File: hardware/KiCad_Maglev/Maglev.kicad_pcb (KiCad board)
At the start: 2 copper layers, 120 x 120 mm, 69 parts, among them IC1 TLV1117LV33DCYR, J1 USB_C_Receptacle, J2 62100421921, J3 61300311121, J4 694106301002, J5 621008245821, J6 621006245821, U1 ESP32-C3, U2 TMAG5173A2QDBVRQ1, Y2 IQXC-42_830108213209

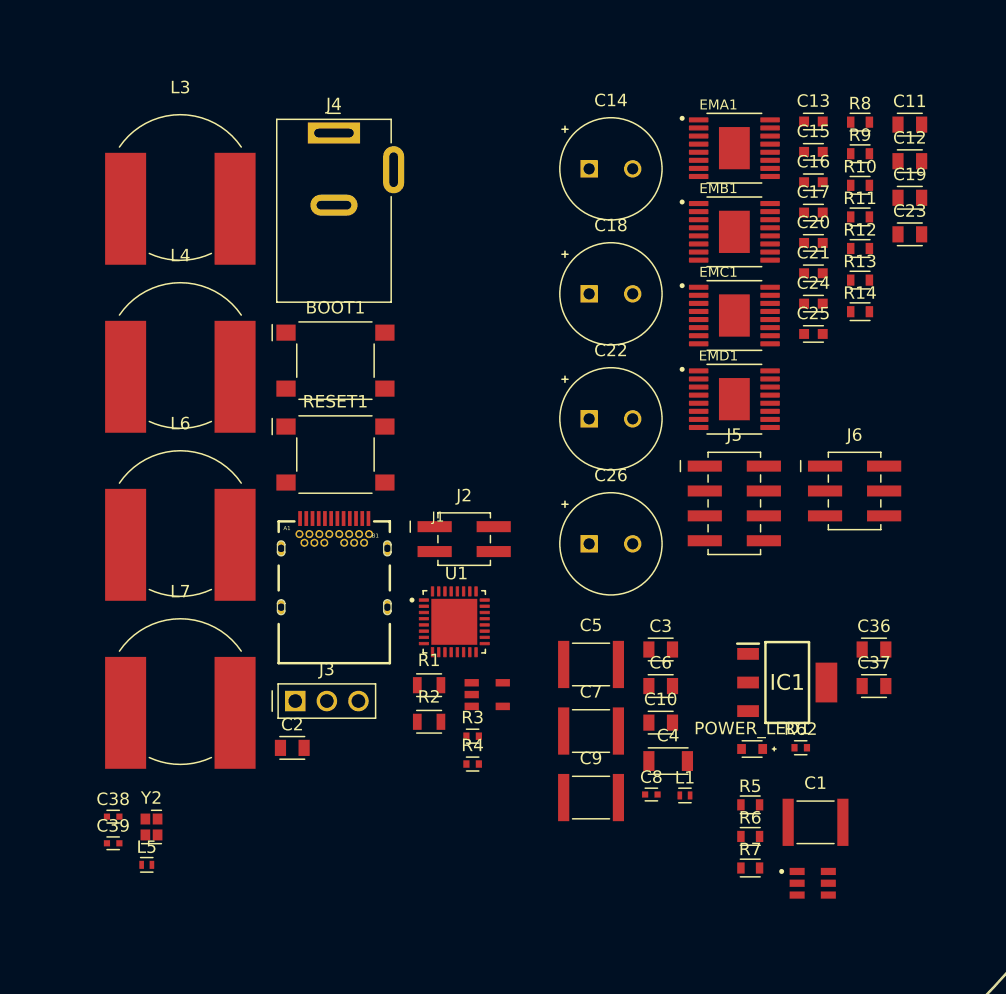
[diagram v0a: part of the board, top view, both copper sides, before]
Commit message: some changes to pcb schmatic, added datasheets for used components and linked wurth repo
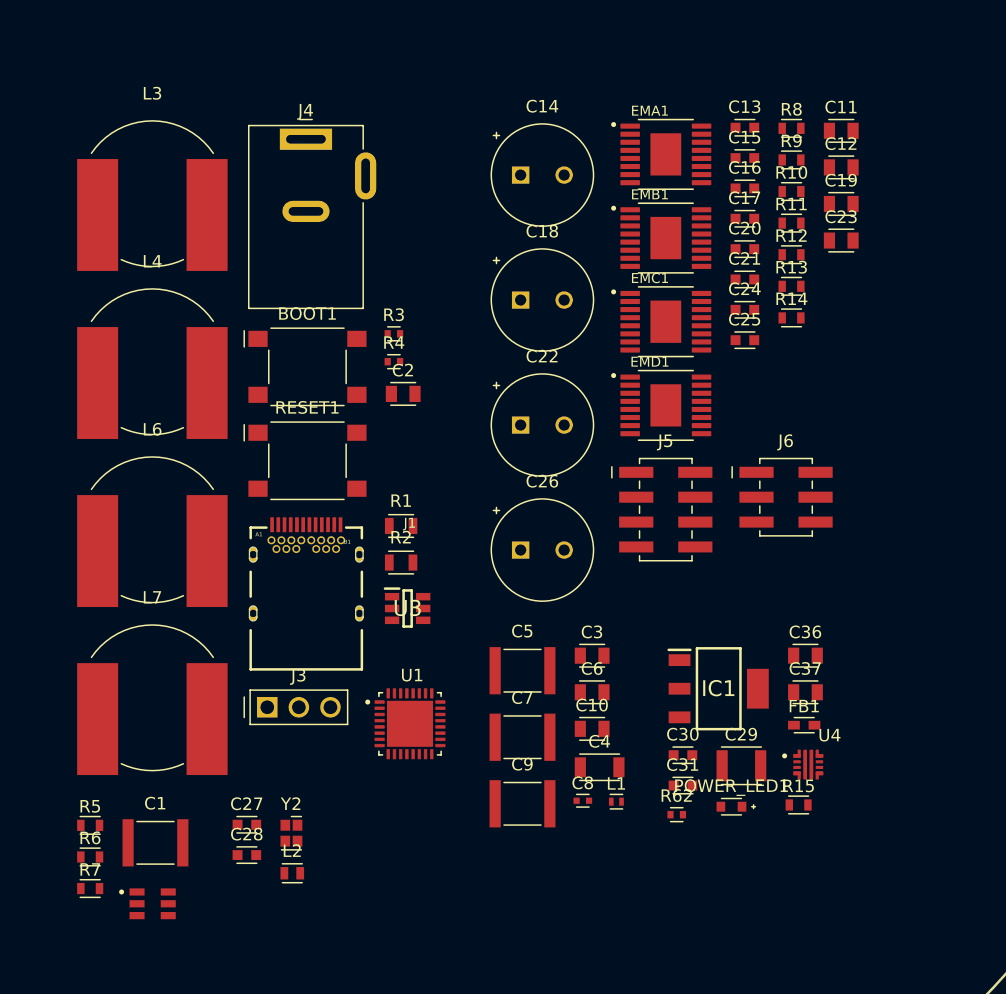
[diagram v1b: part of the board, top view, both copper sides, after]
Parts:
- removed C38, C39: 0402_885012005007, Capacitor_SMD_Wurth:C_Wurth_WCAP-CSGP-0402
- removed D1: 824011, SOT95P280X116-5N:SOT95P280X116-5N
- removed J2: 62100421921, Connector_SMD_Wurth:J_Wurth_WR-PHD_62100421921
- removed L5: 0402_744765124A, Inductor_SMD_Wurth:L_Wurth_WE-KI-0402
- added C27: 0603_R_885012006002, Capacitor_SMD_Wurth:C_Wurth_WCAP-CSGP-0603_R, F.Cu at (133.9, 127.8)
- added C28: 0603_R_885012006002, Capacitor_SMD_Wurth:C_Wurth_WCAP-CSGP-0603_R, F.Cu at (133.9, 130.2)
- added C29: 1210_H2.5_885012209006, Capacitor_SMD_Wurth:C_Wurth_WCAP-CSGP-1210_H2.5, F.Cu at (173.7, 123.0)
- added C30: 0603_R_885012006044, Capacitor_SMD_Wurth:C_Wurth_WCAP-CSGP-0603_R, F.Cu at (169.0, 122.2)
- added C31: 0603_R_885012006017, Capacitor_SMD_Wurth:C_Wurth_WCAP-CSGP-0603_R, F.Cu at (169.0, 124.6)
- added FB1: 0603_W2.6_742792641, Ferrite_SMD_Wurth:FB_Wurth_WE-CBF-0603_W2.6, F.Cu at (178.7, 119.8)
- added L2: 0603_744761124A, Inductor_SMD_Wurth:L_Wurth_WE-KI-0603, F.Cu at (137.6, 131.7)
- added R15: 0603_R_560112116101, Resistor_SMD_Wurth:R_Wurth_WRIS-RSKS-0603_R, F.Cu at (178.3, 126.2)
- added U3: WE-TVS-82400102, SOT95P280X116-6N:SOT95P280X116-6N, F.Cu at (146.8, 110.4)
- added U4: TPS259474ARPWR, IC_TPS259474ARPWR:IC_TPS259474ARPWR, F.Cu at (179.1, 122.9)
- moved C1 53.1 mm to (126.6, 129.2)
- moved R5 53.1 mm to (121.3, 127.8)
- moved R6 53.1 mm to (121.3, 130.3)
- moved R7 53.1 mm to (121.3, 132.9)
- moved U2 53.1 mm to (126.3, 134.1)
- moved R3 33.0 mm to (145.7, 88.3)
- moved R4 33.0 mm to (145.7, 90.5)
- moved C2 29.8 mm to (146.5, 93.1)
- moved R1 13.0 mm to (146.3, 103.7)
- moved R2 13.0 mm to (146.3, 106.7)
- moved R62 11.3 mm to (168.5, 127.0)
- moved Y2 11.3 mm to (137.5, 128.4)
- moved U1 8.94 mm to (147.0, 119.6)
- moved J5 5.53 mm to (167.6, 102.4)
- moved L1 5.53 mm to (163.6, 125.9)
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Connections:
- net /40 MHz Oscillator/-XTAL_40MHz renamed /-XTAL_40_MHz
- net /ESP32 Power Circuit/VDD3P3 renamed /VDD3P3
- net /Electromagnet Driver/EM_POWER renamed +5VP
- J1 pad A4: +5V -> /USB Power Circuit/USB_VBUS
- J1 pad A9: +5V -> /USB Power Circuit/USB_VBUS
- J1 pad B4: +5V -> /USB Power Circuit/USB_VBUS
- J1 pad B9: +5V -> /USB Power Circuit/USB_VBUS
- J3 pad 1: unconnected-(J3-Pad1) -> GND
- J3 pad 2: unconnected-(J3-Pad2) -> GND
- J3 pad 3: unconnected-(J3-Pad3) -> GND
- J4 pad 1: unconnected-(J4-Pad1) -> GND
- J4 pad 2: unconnected-(J4-Pad2) -> GND
- J4 pad 3: unconnected-(J4-Pad3) -> GND
- U1 pad 27: Net-(U1-U0RXD/GPIO20) -> /RXD
- U1 pad 28: Net-(U1-U0TXD/GPIO21) -> /TXD
- U1 pad 30: /40 MHz Oscillator/+XTAL_40MHz -> /+XTAL_40_MHz

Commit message: Added Footprints/Models for coil and ringmagnet, changed most components to 1206 series
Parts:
- removed C36, C37: 0805_H1.25_R_885012107015, Capacitor_SMD_Wurth:C_Wurth_WCAP-CSGP-0805_H1.25_R
- removed L7: 1212_7449152111, Inductor_SMD_Wurth:L_Wurth_WE-ACHC-1212_7449152111
- removed R62: 0402_560112110016, Resistor_SMD_Wurth:R_Wurth_WRIS-RSKS-0402
- removed Y2: IQXC-42_830108213209, Crystal_SMD_Wurth:Y_Wurth_WE-XTAL_Quartz-IQXC-42
- added C32: 0603_R_885012006002, Capacitor_SMD_Wurth:C_Wurth_WCAP-CSGP-0603_R, F.Cu at (237.5, 139.5)
- added C33: 0603_R_885012006002, Capacitor_SMD_Wurth:C_Wurth_WCAP-CSGP-0603_R, F.Cu at (237.5, 141.9)
- added J10: 61300311121, Connector_THT_Wurth:J_Wurth_WR-PHD_61300311121, F.Cu at (219.5, 131.4)
- added J11: 61300211121, Connector_THT_Wurth:J_Wurth_WR-PHD_61300211121, F.Cu at (199.9, 131.4)
- added J12: 61300211121, Connector_THT_Wurth:J_Wurth_WR-PHD_61300211121, F.Cu at (199.9, 136.0)
- added J13: 61300211121, Connector_THT_Wurth:J_Wurth_WR-PHD_61300211121, F.Cu at (199.9, 140.6)
- added J14: 61300511121, Connector_THT_Wurth:J_Wurth_WR-PHD_61300511121, F.Cu at (207.2, 126.8)
- added J15: 61300411121, Connector_THT_Wurth:J_Wurth_WR-PHD_61300411121, F.Cu at (207.2, 131.4)
- added J16: 61300411121, Connector_THT_Wurth:J_Wurth_WR-PHD_61300411121, F.Cu at (207.2, 136.0)
- added J17: 61300411121, Connector_THT_Wurth:J_Wurth_WR-PHD_61300411121, F.Cu at (207.2, 140.6)
- added J2: 691103110002, 691103110002:691103110002, F.Cu at (256.9, 94.2)
- added J7: 61300211121, Connector_THT_Wurth:J_Wurth_WR-PHD_61300211121, F.Cu at (199.9, 122.2)
- added J8: 61300211121, Connector_THT_Wurth:J_Wurth_WR-PHD_61300211121, F.Cu at (199.9, 126.8)
- added J9: 61300811121, Connector_THT_Wurth:J_Wurth_WR-PHD_61300811121, F.Cu at (207.2, 122.2)
- added L5: 0603_744761020A, Inductor_SMD_Wurth:L_Wurth_WE-KI-0603, F.Cu at (242.8, 111.7)
- added POWER_LED2: 0603dome_150060VS86000, LED_SMD_Wurth:D_Wurth_WL-SMCW-0603dome, F.Cu at (254.1, 123.8)
- added R16: 1206_R_560112132019, Resistor_SMD_Wurth:R_Wurth_WRIS-RSKS-1206_R, F.Cu at (219.6, 92.3)
- added R17: 1206_R_560112132019, Resistor_SMD_Wurth:R_Wurth_WRIS-RSKS-1206_R, F.Cu at (219.6, 95.6)
- added R18: 0603_R_560112116101, Resistor_SMD_Wurth:R_Wurth_WRIS-RSKS-0603_R, F.Cu at (258.5, 122.2)
- added R19: 0402_560112110016, Resistor_SMD_Wurth:R_Wurth_WRIS-RSKS-0402, F.Cu at (258.1, 124.6)
- added Status_LED_RX1: 0603dome_150060VS86000, LED_SMD_Wurth:D_Wurth_WL-SMCW-0603dome, F.Cu at (261.3, 102.3)
- added Status_LED_TX1: 0603dome_150060VS86000, LED_SMD_Wurth:D_Wurth_WL-SMCW-0603dome, F.Cu at (261.3, 104.8)
- added U5: TPS259474ARPWR, IC_TPS259474ARPWR:IC_TPS259474ARPWR, F.Cu at (254.7, 120.6)
- added Y1: IQXC-42_830108213209, Crystal_SMD_Wurth:Y_Wurth_WE-XTAL_Quartz-IQXC-42, F.Cu at (241.0, 140.2)
- C1, C5, C9: value 1812_H1.25_885012210008 -> 1206_H1.6_885012208093; footprint Capacitor_SMD_Wurth:C_Wurth_WCAP-CSGP-1812_H1.25 -> Capacitor_SMD_Wurth:C_Wurth_WCAP-CSGP-1206_H1.6
- C10: value 0805_H1.25_R_885012107015 -> 1206_H1.25_885012208118; footprint Capacitor_SMD_Wurth:C_Wurth_WCAP-CSGP-0805_H1.25_R -> Capacitor_SMD_Wurth:C_Wurth_WCAP-CSGP-1206_H1.25
- C11, C12, C19: value 0805_H1.25_R_885342207011 -> 1206_H0.8_885012208083; footprint Capacitor_SMD_Wurth:C_Wurth_WCAP-CSMH-0805_H1.25_R -> Capacitor_SMD_Wurth:C_Wurth_WCAP-CSGP-1206_H0.8
- C13, C15, C16, C21, C24: value 0603_R_885012206095 -> 1206_H1.25_885012208118; footprint Capacitor_SMD_Wurth:C_Wurth_WCAP-CSGP-0603_R -> Capacitor_SMD_Wurth:C_Wurth_WCAP-CSGP-1206_H1.25
- C14, C22: value D8L11.5_870585774003 -> 1206_H1.25_885012208118; footprint Capacitor_THT_Wurth:CP_Wurth_WCAP-HTAH-D8L11.5 -> Capacitor_SMD_Wurth:C_Wurth_WCAP-CSGP-1206_H1.25
- C17, C25: value 0603_R_885012206095 -> D8L11.5_870585774003; footprint Capacitor_SMD_Wurth:C_Wurth_WCAP-CSGP-0603_R -> Capacitor_THT_Wurth:CP_Wurth_WCAP-HTAH-D8L11.5
- C2: value 0805_H1.25_R_885012107015 -> 1206_H1.6_885012208093; footprint Capacitor_SMD_Wurth:C_Wurth_WCAP-CSGP-0805_H1.25_R -> Capacitor_SMD_Wurth:C_Wurth_WCAP-CSGP-1206_H1.6
- C20: value 0603_R_885012206095 -> 1206_H0.8_885012208083; footprint Capacitor_SMD_Wurth:C_Wurth_WCAP-CSGP-0603_R -> Capacitor_SMD_Wurth:C_Wurth_WCAP-CSGP-1206_H0.8
- C23: value 0805_H1.25_R_885342207011 -> 1206_H1.25_885012208118; footprint Capacitor_SMD_Wurth:C_Wurth_WCAP-CSMH-0805_H1.25_R -> Capacitor_SMD_Wurth:C_Wurth_WCAP-CSGP-1206_H1.25
- C27: value 0603_R_885012006002 -> 1206_H1.6_885012208093; footprint Capacitor_SMD_Wurth:C_Wurth_WCAP-CSGP-0603_R -> Capacitor_SMD_Wurth:C_Wurth_WCAP-CSGP-1206_H1.6
- C28: value 0603_R_885012006002 -> 1206_H0.8_885012008001; footprint Capacitor_SMD_Wurth:C_Wurth_WCAP-CSGP-0603_R -> Capacitor_SMD_Wurth:C_Wurth_WCAP-CSGP-1206_H0.8
- C29: value 1210_H2.5_885012209006 -> 1206_H1.6_885012208093; footprint Capacitor_SMD_Wurth:C_Wurth_WCAP-CSGP-1210_H2.5 -> Capacitor_SMD_Wurth:C_Wurth_WCAP-CSGP-1206_H1.6
- C3: value 0805_H1.25_R_885012107015 -> 1206_H1.6_885012108021; footprint Capacitor_SMD_Wurth:C_Wurth_WCAP-CSGP-0805_H1.25_R -> Capacitor_SMD_Wurth:C_Wurth_WCAP-CSGP-1206_H1.6
- C30: value 0603_R_885012006044 -> 1206_H1.6_885342008003; footprint Capacitor_SMD_Wurth:C_Wurth_WCAP-CSGP-0603_R -> Capacitor_SMD_Wurth:C_Wurth_WCAP-CSMH-1206_H1.6
- C31: value 0603_R_885012006017 -> 1206_H1.6_885012108003; footprint Capacitor_SMD_Wurth:C_Wurth_WCAP-CSGP-0603_R -> Capacitor_SMD_Wurth:C_Wurth_WCAP-CSGP-1206_H1.6
- C4: value 1206_H1.6_885012108021 -> 1206_H1.25_885012208118; footprint Capacitor_SMD_Wurth:C_Wurth_WCAP-CSGP-1206_H1.6 -> Capacitor_SMD_Wurth:C_Wurth_WCAP-CSGP-1206_H1.25
- C6: value 0805_H1.25_R_885012107015 -> 1206_H1.25_885012008055; footprint Capacitor_SMD_Wurth:C_Wurth_WCAP-CSGP-0805_H1.25_R -> Capacitor_SMD_Wurth:C_Wurth_WCAP-CSGP-1206_H1.25
- C7: value 1812_H1.25_885012210008 -> 1206_H1.25_885012208118; footprint Capacitor_SMD_Wurth:C_Wurth_WCAP-CSGP-1812_H1.25 -> Capacitor_SMD_Wurth:C_Wurth_WCAP-CSGP-1206_H1.25
- C8: value 0402_885012205050 -> 1206_H1.25_885012208118; footprint Capacitor_SMD_Wurth:C_Wurth_WCAP-CSGP-0402 -> Capacitor_SMD_Wurth:C_Wurth_WCAP-CSGP-1206_H1.25
- J3: value 61300311121 -> 61300621121; footprint Connector_THT_Wurth:J_Wurth_WR-PHD_61300311121 -> Connector_THT_Wurth:J_Wurth_WR-PHD_61300621121
- J4: value 694106301002 -> 61300821121; footprint Connector_THT_Wurth:J_Wurth_WR-DC_694106301002 -> Connector_THT_Wurth:J_Wurth_WR-PHD_61300821121
- J5: value 621008245821 -> 61300821121; footprint Connector_SMD_Wurth:J_Wurth_WR-PHD_621008245821 -> Connector_THT_Wurth:J_Wurth_WR-PHD_61300821121
- J6: value 621006245821 -> 61300621121; footprint Connector_SMD_Wurth:J_Wurth_WR-PHD_621006245821 -> Connector_THT_Wurth:J_Wurth_WR-PHD_61300621121
- L1: value 0402_744765020A -> ElectromagneticActor; footprint Inductor_SMD_Wurth:L_Wurth_WE-KI-0402 -> CUSTOM:EM; moved to B.Cu
- L2: value 0603_744761124A -> ElectromagneticActor; footprint Inductor_SMD_Wurth:L_Wurth_WE-KI-0603 -> CUSTOM:EM; moved to B.Cu
- L3, L4: value 1212_7449152111 -> ElectromagneticActor; footprint Inductor_SMD_Wurth:L_Wurth_WE-ACHC-1212_7449152111 -> CUSTOM:EM; moved to B.Cu
- L6: value 1212_7449152111 -> 0603_744761124A; footprint Inductor_SMD_Wurth:L_Wurth_WE-ACHC-1212_7449152111 -> Inductor_SMD_Wurth:L_Wurth_WE-KI-0603
- R10: value 0603_R_560112116005 -> 1206_R_560112132020; footprint Resistor_SMD_Wurth:R_Wurth_WRIS-RSKS-0603_R -> Resistor_SMD_Wurth:R_Wurth_WRIS-RSKS-1206_R
- R11: value 0603_R_560112116098 -> 1206_R_560112132018; footprint Resistor_SMD_Wurth:R_Wurth_WRIS-RSKS-0603_R -> Resistor_SMD_Wurth:R_Wurth_WRIS-RSKS-1206_R
- R12, R13: value 0603_R_560112116098 -> 1206_R_560112132019; footprint Resistor_SMD_Wurth:R_Wurth_WRIS-RSKS-0603_R -> Resistor_SMD_Wurth:R_Wurth_WRIS-RSKS-1206_R
- R14: value 0603_R_560112116098 -> 1206_R_560112132041; footprint Resistor_SMD_Wurth:R_Wurth_WRIS-RSKS-0603_R -> Resistor_SMD_Wurth:R_Wurth_WRIS-RSKS-1206_R
- R15: value 0603_R_560112116101 -> 0603_R_560112116048
- R3, R4: value 0402_560112110020 -> 1206_R_560112132018; footprint Resistor_SMD_Wurth:R_Wurth_WRIS-RSKS-0402 -> Resistor_SMD_Wurth:R_Wurth_WRIS-RSKS-1206_R
- R5, R6, R7: value 0603_R_560112116006 -> 1206_R_560112132050; footprint Resistor_SMD_Wurth:R_Wurth_WRIS-RSKS-0603_R -> Resistor_SMD_Wurth:R_Wurth_WRIS-RSKS-1206_R
- R8: value 0603_R_560112116015 -> 1206_R_560112132020; footprint Resistor_SMD_Wurth:R_Wurth_WRIS-RSKS-0603_R -> Resistor_SMD_Wurth:R_Wurth_WRIS-RSKS-1206_R
- R9: value 0603_R_560112116048 -> 1206_R_560112132020; footprint Resistor_SMD_Wurth:R_Wurth_WRIS-RSKS-0603_R -> Resistor_SMD_Wurth:R_Wurth_WRIS-RSKS-1206_R
- U1: value ESP32-C3 -> WE-TVS-82400102; footprint ESP32-C3FH4:QFN50P500X500X90-33N -> SOT95P280X116-6N:SOT95P280X116-6N
- U2: value TMAG5173A2QDBVRQ1 -> ESP32-C3; footprint SOT95P280X145-6N:SOT95P280X145-6N -> ESP32-C3FH4:QFN50P500X500X90-33N
- U3: value WE-TVS-82400102 -> ~; footprint SOT95P280X116-6N:SOT95P280X116-6N -> CUSTOM:MagnetRing; moved to B.Cu
- U4: value TPS259474ARPWR -> TMAG5173A2QDBVRQ1; footprint IC_TPS259474ARPWR:IC_TPS259474ARPWR -> SOT95P280X145-6N:SOT95P280X145-6N
- moved C1 141.9 mm to (261.9, 86.6)
- moved U2 141.9 mm to (258.1, 81.4)
- moved R5 131.5 mm to (249.4, 98.1)
- moved R6 131.3 mm to (249.4, 101.3)
- moved R7 131.2 mm to (249.4, 104.5)
- moved L6 120.8 mm to (241.1, 143.4)
- moved J3 120.2 mm to (254.5, 101.0)
- moved R1 120.0 mm to (263.7, 79.2)
- moved R2 120.0 mm to (263.7, 82.2)
- moved C27 116.5 mm to (249.3, 112.0)
- moved C28 116.4 mm to (249.3, 115.2)
- moved U1 114.2 mm to (256.6, 87.2)
- moved J4 110.7 mm to (249.1, 80.0)
- moved R4 103.7 mm to (249.4, 94.8)
- moved R3 103.7 mm to (249.4, 91.6)
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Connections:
- C1 pad 1: GND -> /CHIP_EN
- C1 pad 2: +3.3V -> GND
- C10 pad 1: /VDD3P3 -> +3.3V
- C12 pad 1: Net-(EMB1-CPH) -> Net-(EMC1-CPH)
- C12 pad 2: Net-(EMB1-CPL) -> Net-(EMC1-CPL)
- C13 pad 1: +5VP -> Net-(EMA1-VCP)
- C13 pad 2: GND -> +V_HB
- C14 pad 1: +5VP -> Net-(EMC1-VCP)
- C14 pad 2: GND -> +V_HB
- C15 pad 1: +5VP -> +V_HB
- C15 pad 2: Net-(EMA1-VCP) -> GND
- C16 pad 1: +5VP -> +V_HB
- C16 pad 2: Net-(EMB1-VCP) -> GND
- C17 pad 1: +5VP -> +V_HB
- C18 pad 1: +5VP -> +V_HB
- C19 pad 1: Net-(EMC1-CPH) -> Net-(EMB1-CPH)
- C19 pad 2: Net-(EMC1-CPL) -> Net-(EMB1-CPL)
- C2 pad 1: /CHIP_EN -> +3.3V
- C20 pad 1: +5VP -> Net-(EMD1-CPH)
- C20 pad 2: Net-(EMC1-VCP) -> Net-(EMD1-CPL)
- C21 pad 1: +5VP -> Net-(EMB1-VCP)
- C21 pad 2: GND -> +V_HB
- C22 pad 1: +5VP -> Net-(EMD1-VCP)
- C22 pad 2: GND -> +V_HB
- C23 pad 1: Net-(EMD1-CPH) -> +V_HB
- C23 pad 2: Net-(EMD1-CPL) -> GND
- C24 pad 1: +5VP -> +V_HB
- C24 pad 2: Net-(EMD1-VCP) -> GND
- C25 pad 1: +5VP -> +V_HB
- C26 pad 1: +5VP -> +V_HB
- C27 pad 1: GND -> +5V
- C27 pad 2: /-XTAL_40_MHz -> GND
- C28 pad 1: GND -> Net-(U5-ITIMER)
- C28 pad 2: Net-(C28-Pad2) -> GND
- C29 pad 1: +5VP -> +3.3V
- C30 pad 1: Net-(U4-DVDT) -> Net-(U5-DVDT)
- C31 pad 1: Net-(U4-ITIMER) -> +5VP
- C9 pad 1: +3.3V -> /VDD3P3
- EMA1 pad 11: +5VP -> +V_HB
- EMB1 pad 11: +5VP -> +V_HB
- EMC1 pad 11: +5VP -> +V_HB
- EMD1 pad 11: +5VP -> +V_HB
- J3 pad 1: GND -> unconnected-(J3-Pad1)
- J3 pad 2: GND -> unconnected-(J3-Pad2)
- J3 pad 3: GND -> +5VP
- J4 pad 1: GND -> Net-(J4-Pad1)
- J4 pad 2: GND -> Net-(U2-U0RXD/GPIO20)
- J4 pad 3: GND -> /RXD
- J5 pad 2: /Electromagnet Driver/IMODE -> unconnected-(J5-Pad2)
- L1 pad 1: +3.3V -> /Electromagnet Driver/EM_A_N
- L1 pad 2: /VDD3P3 -> /Electromagnet Driver/EM_A_P
- L2 pad 1: Net-(C28-Pad2) -> /Electromagnet Driver/EM_B_N
- L2 pad 2: /+XTAL_40_MHz -> /Electromagnet Driver/EM_B_P
- L3 pad 1: /Electromagnet Driver/EM_B_P -> /Electromagnet Driver/EM_C_N
- L3 pad 2: /Electromagnet Driver/EM_B_N -> /Electromagnet Driver/EM_C_P
- L4 pad 1: /Electromagnet Driver/EM_A_P -> /Electromagnet Driver/EM_D_N
- L4 pad 2: /Electromagnet Driver/EM_A_N -> /Electromagnet Driver/EM_D_P
- L6 pad 1: /Electromagnet Driver/EM_C_P -> Net-(C33-Pad2)
- L6 pad 2: /Electromagnet Driver/EM_C_N -> /+XTAL_40_MHz
- POWER_LED1 pad 1: GND -> /BOOT
- R10 pad 2: GND -> /I2C_INT
- R11 pad 1: /HBRIDGE_A_ISENSE -> +3.3V
- R12 pad 1: /HBRIDGE_B_ISENSE -> /HBRIDGE_A_ISENSE
- R14 pad 1: /HBRIDGE_D_ISENSE -> GND
- R14 pad 2: GND -> Net-(J5-Pad3)
- R15 pad 1: Net-(U4-ILM) -> GND
- R15 pad 2: GND -> Net-(J5-Pad7)
- R5 pad 2: /I2C_SCL -> Net-(POWER_LED1-+)
- R6 pad 1: +3.3V -> Net-(J4-Pad1)
- R6 pad 2: /I2C_SDA -> Net-(Status_LED_RX1-+)
- R7 pad 1: +3.3V -> Net-(J4-Pad5)
- R7 pad 2: /I2C_INT -> Net-(Status_LED_TX1-+)
- R8 pad 1: GND -> +3.3V
- R8 pad 2: Net-(J5-Pad3) -> /I2C_SCL
- R9 pad 1: GND -> +3.3V
- R9 pad 2: Net-(J5-Pad7) -> /I2C_SDA
- U1 pad 1: unconnected-(U1-LNA_IN-Pad1) -> Net-(J1-D+-PadA6)
- U1 pad 2: /VDD3P3 -> GND
- U1 pad 3: /VDD3P3 -> /+USB_D
- U1 pad 4: /HBRIDGE_A_ISENSE -> /-USB_D
- U1 pad 5: /HBRIDGE_B_ISENSE -> /USB Power Circuit/USB_VBUS
- U1 pad 6: /HBRIDGE_C_ISENSE -> Net-(J1-D--PadA7)
- U2 pad 1: /I2C_SCL -> unconnected-(U2-LNA_IN-Pad1)
- U2 pad 2: GND -> /VDD3P3
- U2 pad 3: GND -> /VDD3P3
- U2 pad 4: +3.3V -> /HBRIDGE_A_ISENSE
- U2 pad 5: /I2C_INT -> /HBRIDGE_B_ISENSE
- U2 pad 6: /I2C_SDA -> /HBRIDGE_C_ISENSE
- U4 pad 1: /USB Power Circuit/USB_VBUS -> /I2C_SCL
- U4 pad 2: unconnected-(U4-OVLO-Pad2) -> GND
- U4 pad 3: unconnected-(U4-PG-Pad3) -> GND
- U4 pad 4: unconnected-(U4-PGTH-Pad4) -> +3.3V
- U4 pad 5: /USB Power Circuit/USB_VBUS -> /I2C_INT
- U4 pad 6: +5VP -> /I2C_SDA
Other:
- board size 120 x 120 mm -> 250 x 120 mm

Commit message: Spacer Footprints added, updated some libraries
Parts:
- removed BOOT1, RESET1: 430182043816, Switch_SMD_Wurth:SW_Wurth_WS-TASV_430182043816
- removed C1, C2, C27, C29, C5, C9: 1206_H1.6_885012208093, Capacitor_SMD_Wurth:C_Wurth_WCAP-CSGP-1206_H1.6
- removed C10, C4, C7, C8: 1206_H1.25_885012208118, Capacitor_SMD_Wurth:C_Wurth_WCAP-CSGP-1206_H1.25
- removed C28: 1206_H0.8_885012008001, Capacitor_SMD_Wurth:C_Wurth_WCAP-CSGP-1206_H0.8
- removed C3: 1206_H1.6_885012108021, Capacitor_SMD_Wurth:C_Wurth_WCAP-CSGP-1206_H1.6
- removed C30: 1206_H1.6_885342008003, Capacitor_SMD_Wurth:C_Wurth_WCAP-CSMH-1206_H1.6
- removed C31: 1206_H1.6_885012108003, Capacitor_SMD_Wurth:C_Wurth_WCAP-CSGP-1206_H1.6
- removed C32, C33: 0603_R_885012006002, Capacitor_SMD_Wurth:C_Wurth_WCAP-CSGP-0603_R
- removed C6: 1206_H1.25_885012008055, Capacitor_SMD_Wurth:C_Wurth_WCAP-CSGP-1206_H1.25
- removed FB1: 0603_W2.6_742792641, Ferrite_SMD_Wurth:FB_Wurth_WE-CBF-0603_W2.6
- removed IC1: TLV1117LV33DCYR, SOT230P700X180-4N:SOT230P700X180-4N
- removed J1: USB_C_Receptacle, WURTH_USB:632723300011
- removed J10: 61300311121, Connector_THT_Wurth:J_Wurth_WR-PHD_61300311121
- removed J11, J12, J13, J7, J8: 61300211121, Connector_THT_Wurth:J_Wurth_WR-PHD_61300211121
- removed J14: 61300511121, Connector_THT_Wurth:J_Wurth_WR-PHD_61300511121
- removed J15, J16, J17: 61300411121, Connector_THT_Wurth:J_Wurth_WR-PHD_61300411121
- removed J2: 691103110002, 691103110002:691103110002
- removed J3: 61300621121, Connector_THT_Wurth:J_Wurth_WR-PHD_61300621121
- removed J4: 61300821121, Connector_THT_Wurth:J_Wurth_WR-PHD_61300821121
- removed J9: 61300811121, Connector_THT_Wurth:J_Wurth_WR-PHD_61300811121
- removed L5: 0603_744761020A, Inductor_SMD_Wurth:L_Wurth_WE-KI-0603
- removed L6: 0603_744761124A, Inductor_SMD_Wurth:L_Wurth_WE-KI-0603
- removed POWER_LED1, POWER_LED2, Status_LED_RX1, Status_LED_TX1: 0603dome_150060VS86000, LED_SMD_Wurth:D_Wurth_WL-SMCW-0603dome
- removed R1, R2: 0805_R_560112120019, Resistor_SMD_Wurth:R_Wurth_WRIS-RSKS-0805_R
- removed R18: 0603_R_560112116101, Resistor_SMD_Wurth:R_Wurth_WRIS-RSKS-0603_R
- removed R19: 0402_560112110016, Resistor_SMD_Wurth:R_Wurth_WRIS-RSKS-0402
- removed U1: WE-TVS-82400102, SOT95P280X116-6N:SOT95P280X116-6N
- removed U2: ESP32-C3, ESP32-C3FH4:QFN50P500X500X90-33N
- removed U5: TPS259474ARPWR, IC_TPS259474ARPWR:IC_TPS259474ARPWR
- removed Y1: IQXC-42_830108213209, Crystal_SMD_Wurth:Y_Wurth_WE-XTAL_Quartz-IQXC-42
- added Magnet2: ~, CUSTOM:MagnetRing_2, F.Cu at (220.0, 100.0)
- added U10: ~, CUSTOM:Spacer, F.Cu at (165.0, 100.0)
- added U11: ~, CUSTOM:Spacer, B.Cu at (35.0, 100.0)
- added U12: ~, CUSTOM:Spacer, B.Cu at (90.0, 45.0)
- added U13: ~, CUSTOM:Spacer, B.Cu at (90.0, 155.0)
- added U6: ~, CUSTOM:Spacer, F.Cu at (220.0, 45.0)
- added U7: ~, CUSTOM:Spacer, F.Cu at (275.0, 100.0)
- added U8: ~, CUSTOM:Spacer, F.Cu at (220.0, 155.0)
- added U9: ~, CUSTOM:Spacer, B.Cu at (145.0, 100.0)
- C17, EMA1: moved to B.Cu
- moved J6 196.5 mm to (391.0, 30.8)
- moved R15 196.5 mm to (390.5, 39.4)
- moved EMB1 182.4 mm to (384.2, 26.3)
- moved EMC1 182.4 mm to (384.2, 33.1)
- moved EMD1 182.4 mm to (384.2, 39.8)
- moved C18 182.4 mm to (372.5, 31.3)
- moved C25 182.4 mm to (372.5, 41.4)
- moved C26 182.4 mm to (372.5, 51.4)
- moved J5 177.4 mm to (391.0, 18.5)
- moved C23 171.2 mm to (393.2, 51.2)
- moved C11 171.2 mm to (382.1, 44.8)
- moved C12 171.2 mm to (382.1, 48.0)
- moved C13 171.2 mm to (382.1, 51.2)
- moved C14 171.2 mm to (382.1, 54.5)
- moved C15 171.2 mm to (387.6, 44.8)
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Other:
- copper layers 2 -> 4

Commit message: changed mounting and spacing system and  some detail changes
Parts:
- removed U10, U11, U12, U13, U6, U7, U8, U9: ~, CUSTOM:Spacer
- added BOOT1: 430182043816, Switch_SMD_Wurth:SW_Wurth_WS-TASV_430182043816, F.Cu at (186.2, 149.8)
- added C1: 1206_H1.6_885012208093, Capacitor_SMD_Wurth:C_Wurth_WCAP-CSGP-1206_H1.6, B.Cu at (226.3, 122.0)
- added C10: 1206_H1.25_885012208118, Capacitor_SMD_Wurth:C_Wurth_WCAP-CSGP-1206_H1.25, B.Cu at (205.6, 80.4)
- added C2: 1206_H1.6_885012208093, Capacitor_SMD_Wurth:C_Wurth_WCAP-CSGP-1206_H1.6, B.Cu at (231.6, 62.3)
- added C27: 1206_H1.6_885012208093, Capacitor_SMD_Wurth:C_Wurth_WCAP-CSGP-1206_H1.6, B.Cu at (222.7, 72.0)
- added C28: 1206_H0.8_885012008001, Capacitor_SMD_Wurth:C_Wurth_WCAP-CSGP-1206_H0.8, B.Cu at (222.7, 75.2)
- added C29: 1206_H1.6_885012208093, Capacitor_SMD_Wurth:C_Wurth_WCAP-CSGP-1206_H1.6, B.Cu at (222.7, 78.5)
- added C3: 1206_H1.6_885012108021, Capacitor_SMD_Wurth:C_Wurth_WCAP-CSGP-1206_H1.6, B.Cu at (231.6, 65.5)
- added C30: 1206_H1.6_885342008003, Capacitor_SMD_Wurth:C_Wurth_WCAP-CSMH-1206_H1.6, B.Cu at (222.7, 81.7)
- added C31: 1206_H1.6_885012108003, Capacitor_SMD_Wurth:C_Wurth_WCAP-CSGP-1206_H1.6, B.Cu at (222.7, 85.0)
- added C32: 0603_R_885012006002, Capacitor_SMD_Wurth:C_Wurth_WCAP-CSGP-0603_R, B.Cu at (206.4, 71.6)
- added C33: 0603_R_885012006002, Capacitor_SMD_Wurth:C_Wurth_WCAP-CSGP-0603_R, B.Cu at (206.4, 74.0)
- added C4: 1206_H1.25_885012208118, Capacitor_SMD_Wurth:C_Wurth_WCAP-CSGP-1206_H1.25, B.Cu at (231.6, 68.7)
- added C5: 1206_H1.6_885012208093, Capacitor_SMD_Wurth:C_Wurth_WCAP-CSGP-1206_H1.6, B.Cu at (231.6, 72.0)
- added C6: 1206_H1.25_885012008055, Capacitor_SMD_Wurth:C_Wurth_WCAP-CSGP-1206_H1.25, B.Cu at (231.6, 75.2)
- added C7: 1206_H1.25_885012208118, Capacitor_SMD_Wurth:C_Wurth_WCAP-CSGP-1206_H1.25, B.Cu at (231.6, 78.5)
- added C8: 1206_H1.25_885012208118, Capacitor_SMD_Wurth:C_Wurth_WCAP-CSGP-1206_H1.25, B.Cu at (231.6, 81.7)
- added C9: 1206_H1.6_885012208093, Capacitor_SMD_Wurth:C_Wurth_WCAP-CSGP-1206_H1.6, B.Cu at (231.6, 84.9)
- added FB1: 0603_W2.6_742792641, Ferrite_SMD_Wurth:FB_Wurth_WE-CBF-0603_W2.6, B.Cu at (213.3, 79.8)
- added IC1: TLV1117LV33DCYR, SOT230P700X180-4N:SOT230P700X180-4N, B.Cu at (215.2, 74.5)
- added J1: USB_C_Receptacle, WURTH_USB:632723300011, F.Cu at (265.2, 129.0)
- added J2: 691103110002, 691103110002:691103110002, F.Cu at (243.8, 149.8)
- added J3: 61300621121, Connector_THT_Wurth:J_Wurth_WR-PHD_61300621121, B.Cu at (219.5, 94.5)
- added J4: 61300821121, Connector_THT_Wurth:J_Wurth_WR-PHD_61300821121, B.Cu at (226.8, 94.5)
- added L5: 0603_744761020A, Inductor_SMD_Wurth:L_Wurth_WE-KI-0603, B.Cu at (227.1, 62.0)
- added L6: 0603_744761124A, Inductor_SMD_Wurth:L_Wurth_WE-KI-0603, B.Cu at (202.8, 75.5)
- added POWER_LED1: 0603dome_150060VS86000, LED_SMD_Wurth:D_Wurth_WL-SMCW-0603dome, B.Cu at (206.2, 111.5)
- added POWER_LED2: 0603dome_150060VS86000, LED_SMD_Wurth:D_Wurth_WL-SMCW-0603dome, B.Cu at (218.0, 83.8)
- added R1: 0805_R_560112120019, Resistor_SMD_Wurth:R_Wurth_WRIS-RSKS-0805_R, B.Cu at (206.1, 119.0)
- added R18: 0603_R_560112116101, Resistor_SMD_Wurth:R_Wurth_WRIS-RSKS-0603_R, B.Cu at (213.6, 82.2)
- added R19: 0402_560112110016, Resistor_SMD_Wurth:R_Wurth_WRIS-RSKS-0402, B.Cu at (214.0, 84.6)
- added R2: 0805_R_560112120019, Resistor_SMD_Wurth:R_Wurth_WRIS-RSKS-0805_R, B.Cu at (206.1, 122.0)
- added REF**: Electromagnet_2, CUSTOM:Electromagnet_2, F.Cu at (215.0, 119.0)
- added REF**: J_Wurth_WR-MM_690367191672, Connector_THT_Wurth:J_Wurth_WR-MM_690367191672, F.Cu at (168.5, 67.0)
- added REF**: J_Wurth_WR-MM_690367191672, Connector_THT_Wurth:J_Wurth_WR-MM_690367191672, B.Cu at (47.0, 53.5)
- added REF**1: Electromagnet_2, CUSTOM:Electromagnet_2, F.Cu at (196.0, 100.0)
- added REF**2: Electromagnet_2, CUSTOM:Electromagnet_2, F.Cu at (215.0, 81.0)
- added REF**3: Electromagnet_2, CUSTOM:Electromagnet_2, F.Cu at (234.0, 100.0)
- added RESET1: 430182043816, Switch_SMD_Wurth:SW_Wurth_WS-TASV_430182043816, F.Cu at (165.2, 128.8)
- added S1: ~, CUSTOM:Spacer_15mm, B.Cu at (215.0, 45.0)
- added S2: ~, CUSTOM:Spacer_15mm, B.Cu at (160.0, 100.0)
- added S3: ~, CUSTOM:Spacer_15mm, B.Cu at (215.0, 155.0)
- added S4: ~, CUSTOM:Spacer_15mm, B.Cu at (270.0, 100.0)
- added S5: ~, CUSTOM:Spacer_20mm, B.Cu at (80.0, 45.0)
- added S6: ~, CUSTOM:Spacer_20mm, B.Cu at (25.0, 100.0)
- added S7: ~, CUSTOM:Spacer_20mm, B.Cu at (135.0, 100.0)
- added S8: ~, CUSTOM:Spacer_20mm, B.Cu at (80.0, 155.0)
- added Status_LED_RX1: 0603dome_150060VS86000, LED_SMD_Wurth:D_Wurth_WL-SMCW-0603dome, B.Cu at (206.2, 113.9)
- added Status_LED_TX1: 0603dome_150060VS86000, LED_SMD_Wurth:D_Wurth_WL-SMCW-0603dome, B.Cu at (206.2, 116.3)
- added U1: WE-TVS-82400102, SOT95P280X116-6N:SOT95P280X116-6N, B.Cu at (215.3, 121.2)
- added U2: ESP32-C3, ESP32-C3FH4:QFN50P500X500X90-33N, B.Cu at (224.9, 116.8)
- added U5: TPS259474ARPWR, IC_TPS259474ARPWR:IC_TPS259474ARPWR, B.Cu at (217.3, 80.6)
- added Y1: IQXC-42_830108213209, Crystal_SMD_Wurth:Y_Wurth_WE-XTAL_Quartz-IQXC-42, B.Cu at (202.8, 72.3)
- C11, C12, C13, C14, C15, C16, C19, C20, C21, C22, C23, C24, EMB1, EMC1, EMD1, J5, J6, R10, R11, R12, R13, R14, R15, R16, R17, R3, R4, R5, R6, R7, R8, R9: moved to B.Cu
- C17: moved to F.Cu
- L1, L2, L3, L4: footprint CUSTOM:EM -> CUSTOM:Electromagnet
- moved C21 232.1 mm to (162.9, 73.5), turned to 180 degrees
- moved C22 232.1 mm to (162.9, 76.8), turned to 180 degrees
- moved C23 232.1 mm to (162.9, 80.0), turned to 180 degrees
- moved C24 232.1 mm to (162.9, 83.2), turned to 180 degrees
- moved C18 229.6 mm to (157.4, 111.5)
- moved C16 221.1 mm to (168.4, 76.8), turned to 180 degrees
- moved C15 221.1 mm to (168.4, 73.5), turned to 180 degrees
- moved C19 221.1 mm to (168.4, 80.0), turned to 180 degrees
- moved C20 221.1 mm to (168.4, 83.2), turned to 180 degrees
- moved EMD1 216.1 mm to (176.8, 100.4), turned to -90 degrees
- moved C11 210.1 mm to (174.0, 73.5), turned to 180 degrees
- moved C12 210.1 mm to (174.0, 76.8), turned to 180 degrees
- moved C13 210.1 mm to (174.0, 80.0), turned to 180 degrees
- moved C14 210.1 mm to (174.0, 83.2), turned to 180 degrees
- moved R15 208.0 mm to (199.6, 121.9), turned to 180 degrees
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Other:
- board size 250 x 120 mm -> 265 x 130 mm
